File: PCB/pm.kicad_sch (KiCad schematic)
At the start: 22 parts, among them J2 USB_C_Receptacle_USB2.0_14P, J3 Conn_01x02_Socket, Q1 FS8205, SW2 SW_SPDT, U2 TP4057, U3 AP2127K-3.3, U4 DW01A

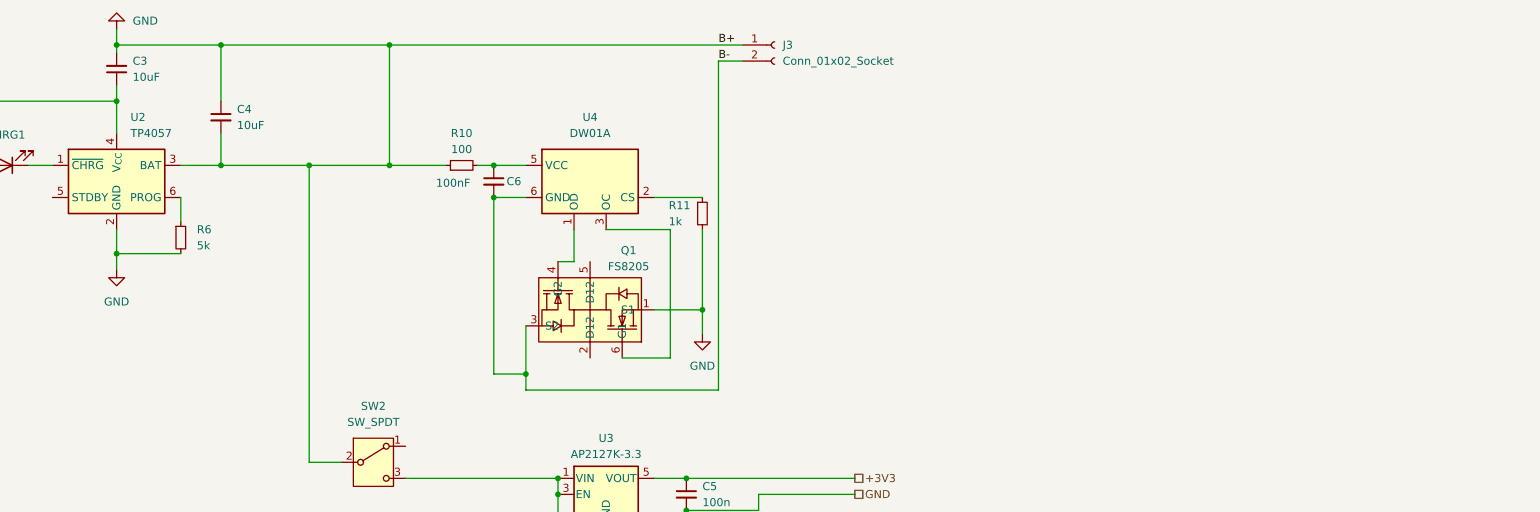
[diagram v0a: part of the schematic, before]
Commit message: Add protection circuit to PCB I don't like the design tho, so let's fix that
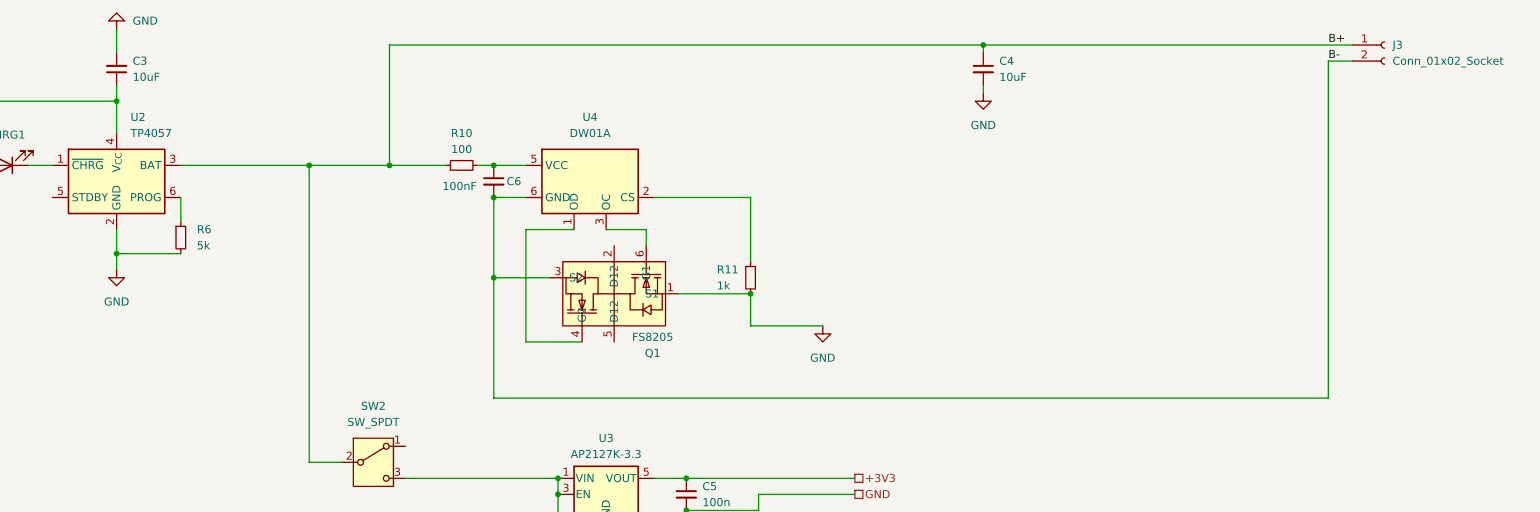
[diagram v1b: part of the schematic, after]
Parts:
- C6: footprint (none) -> Capacitor_SMD:C_0402_1005Metric
- Q1: footprint easyeda2kicad:SOT-23-6_L2.9-W1.6-P0.95-LS2.8-BR -> Package_TO_SOT_SMD:SOT-23-6
- R10, R11: footprint (none) -> Resistor_SMD:R_0402_1005Metric
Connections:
- net GND: no longer C4.1, J3.1 (Pin_1), R10.1, SW2.2 (B), U2.3 (BAT)
- new net B+: C4.1, J3.1 (Pin_1), R10.1, SW2.2 (B), U2.3 (BAT)
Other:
- moved on the sheet: J3, Q1, R11

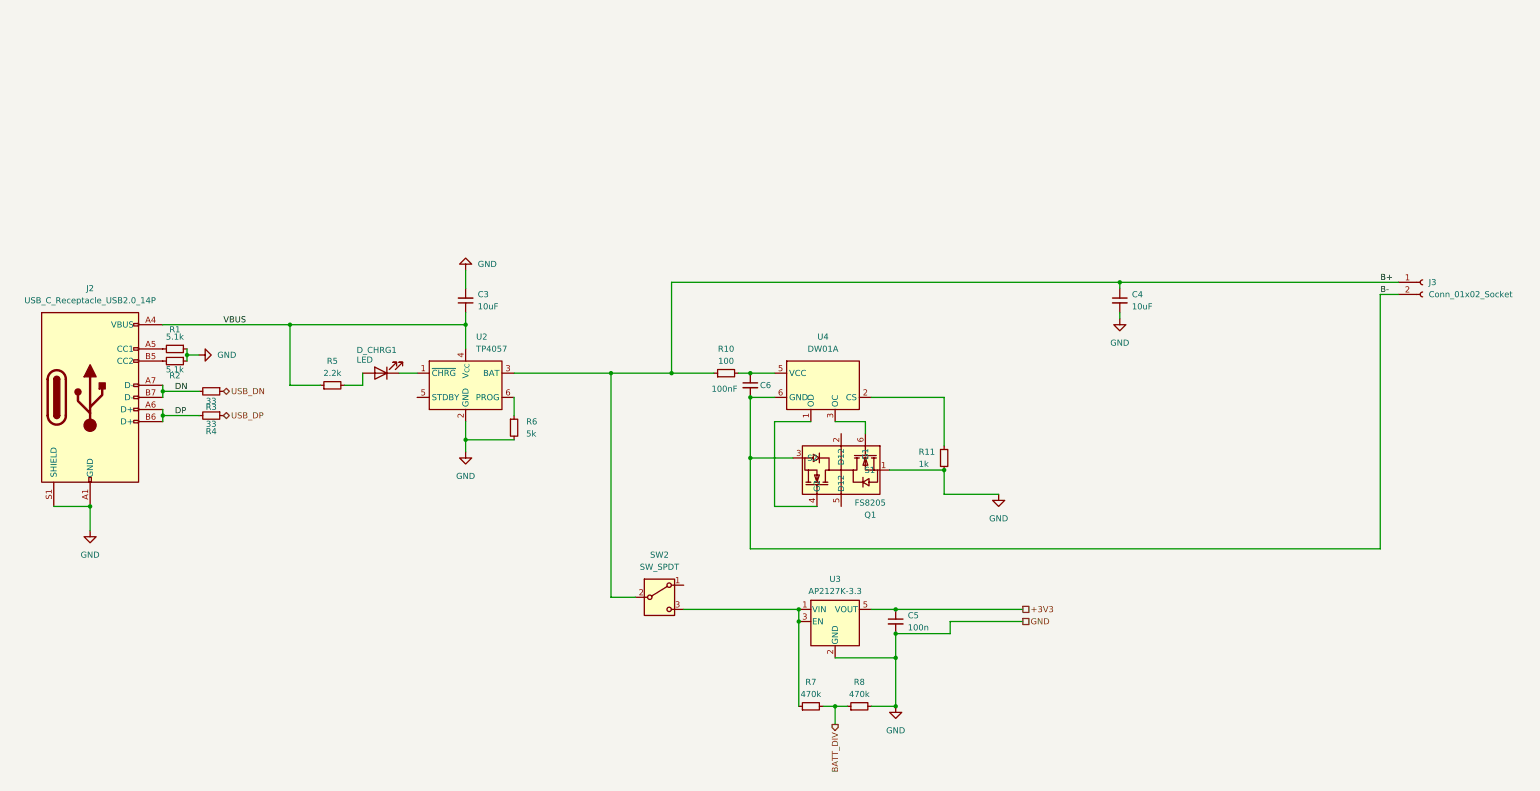
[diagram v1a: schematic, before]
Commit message: Add USBLC6-2P6 for ESD protection The usual COMPLETE REDESIGN because it didn't fit
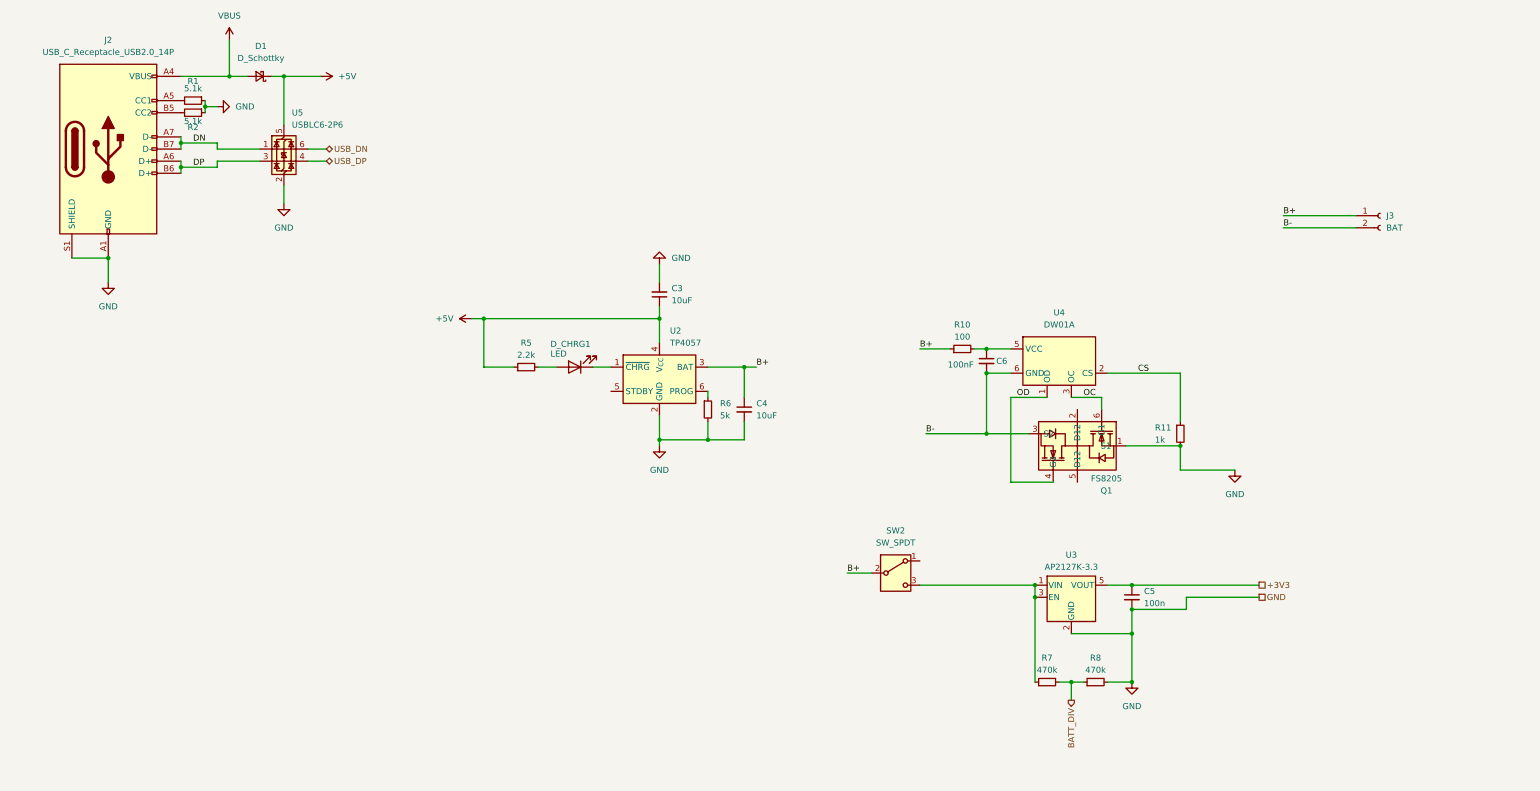
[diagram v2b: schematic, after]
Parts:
- removed R3, R4: 33, Resistor_SMD:R_0402_1005Metric, symbol Device:R_Small
- added D1: D_Schottky, Diode_SMD:D_0402_1005Metric, symbol Device:D_Schottky_Small
- added U5: USBLC6-2P6, Package_TO_SOT_SMD:SOT-666, symbol Power_Protection:USBLC6-2P6
- J3: value Conn_01x02_Socket -> BAT
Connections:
- net DN: now also U5.1 (I/O1)
- net DP: now also U5.3 (I/O2)
- net GND: now also U5.2 (GND)
- net USB_DN: now also U5.6 (I/O1)
- net USB_DP: now also U5.4 (I/O2)
- net VBUS: now also D1.2 (A); no longer C3.1, R5.1, U2.4 (V_{CC})
- net CS: now reaches R11.1, U4.2 (CS)
- net OD: now reaches Q1.4 (G2), U4.1 (OD)
- net OC: now reaches Q1.6 (G1), U4.3 (OC)
- new net +5V: C3.1, D1.1 (K), R5.1, U2.4 (V_{CC}), U5.5 (VBUS)
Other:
- moved on the sheet: C3, C5, C6, D_CHRG1, J2, J3, Q1, R1, R10, R11, R2, R5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

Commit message: Replace 5k with 5.1k resistor Resistor for limiting charging current, it is within tolerance - eliminating one SKU
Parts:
- R6: value 5k -> 5.1k
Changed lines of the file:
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@@
 			)
 		)
-		(property "Value" "5k"
+		(property "Value" "5.1k"
 			(at 167.64 104.1399 0)
 			(effects

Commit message: Change LED resistor value
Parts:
- D_CHRG1: value LED -> RED_LED
- R5: value 2.2k -> 1.5k
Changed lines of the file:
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@@
 			)
 		)
-		(property "Value" "LED"
+		(property "Value" "RED_LED"
 			(at 132.08 91.186 0)
 			(effects
@@
 			)
 		)
-		(property "Value" "2.2k"
+		(property "Value" "1.5k"
 			(at 127 91.44 90)
 			(effects

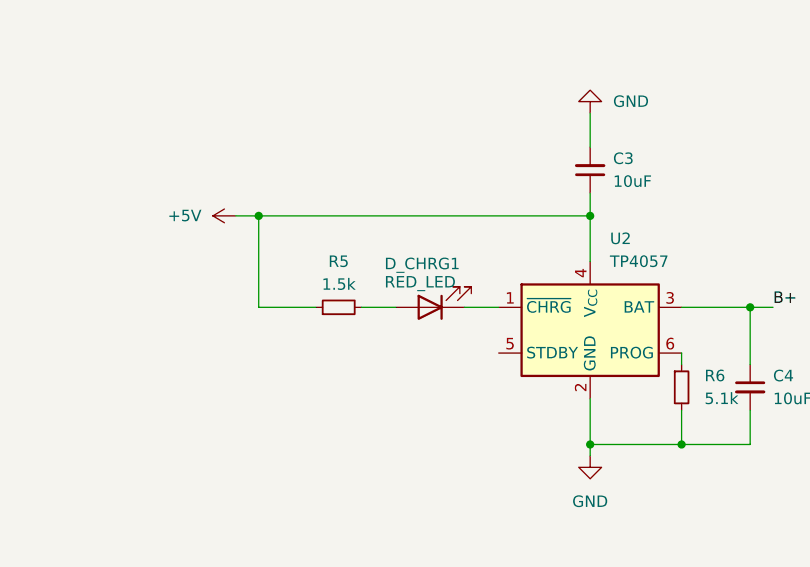
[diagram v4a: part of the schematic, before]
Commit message: Change LED and it's resistor Once again, i found i had this laying around
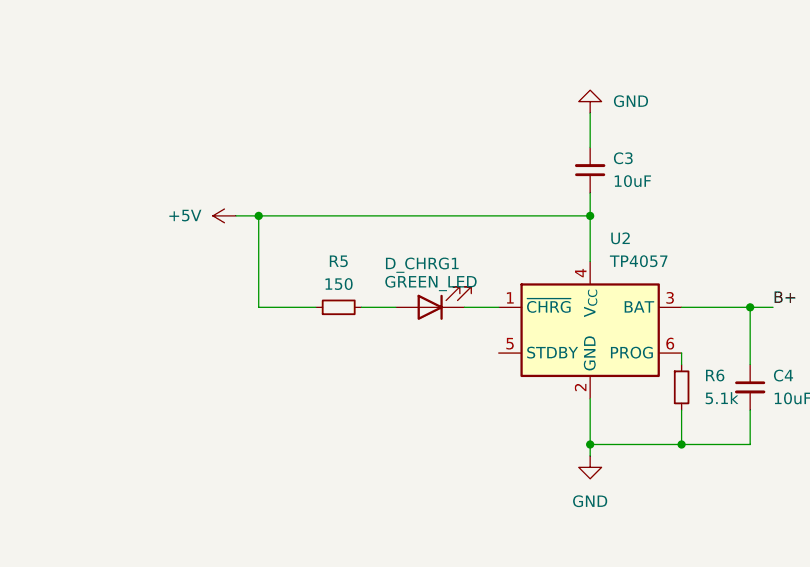
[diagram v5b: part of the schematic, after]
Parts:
- D_CHRG1: value RED_LED -> GREEN_LED
- R5: value 1.5k -> 150
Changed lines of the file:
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@@
 			)
 		)
-		(property "Value" "RED_LED"
+		(property "Value" "GREEN_LED"
 			(at 132.08 91.186 0)
 			(effects
@@
 			)
 		)
-		(property "Value" "1.5k"
+		(property "Value" "150"
 			(at 127 91.44 90)
 			(effects
